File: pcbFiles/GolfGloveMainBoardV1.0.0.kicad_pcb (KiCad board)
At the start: 4 copper layers, 55.3 x 40 mm, 135 parts, among them J1 USB_C_Receptacle, J11 Conn_01x16_Male, J12 HOST_WAKE, J13 TP4, J14 Conn_01x02, J15 Conn_01x02, J16 Conn_01x02, J17 Conn_01x02, J2 Conn_01x06, J3 USB_C_Receptacle, J6 Screw_Terminal_01x02, J7 Conn_01x02, J8 Conn_01x02, J9 Conn_01x02, SW1 SW_SPDT, SW2 SW_Push, U1 MCP73831T-2ACI/OT, U2 XC6119N16A7R-G, U3 LSM9DS1TR, U4 CYW20719B1KUMLG, U5 LSM9DS1TR, U7 TPS63001DRCT, Y1 Crystal, Y3 Crystal_GND24

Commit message: Updates
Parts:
- removed C3, C4: C, Capacitors_SMD:C_0402
- removed J11: Conn_01x16_Male, Pin_Headers:Pin_Header_Straight_2x08_Pitch2.54mm
- removed J12: HOST_WAKE, Pin_Headers:Pin_Header_Straight_1x01_Pitch2.54mm
- removed J13: TP4, Pin_Headers:Pin_Header_Straight_1x01_Pitch2.54mm
- removed U2: XC6119N16A7R-G, DFN-4-------------------------:DFN-4
- added J4: Conn_01x02_Male, Pin_Headers:Pin_Header_Straight_1x02_Pitch2.54mm, F.Cu at (145.6, 147.0)
- added J5: Conn_01x02_Male, Pin_Headers:Pin_Header_Straight_1x02_Pitch2.54mm, F.Cu at (139.3, 146.8)
- added SW3: SW_Push_Dual, Buttons_Switches_THT:SW_PUSH_6mm, F.Cu at (127.5, 116.5)
- C8, C9, R3, R4: moved to F.Cu
- J6: value Screw_Terminal_01x02 -> Conn_01x02_Male
- SW2: footprint Buttons_Switches_SMD:SW_DIP_x1_W8.61mm_Slide_LowProfile -> Buttons_Switches_THT:SW_PUSH_6mm
- Y1: footprint Crystals:Crystal_SMD_0603-2pin_6.0x3.5mm_HandSoldering -> Crystals:Crystal_SMD_3215-2pin_3.2x1.5mm; moved to F.Cu
- Y3: footprint Crystals:Crystal_SMD_0603-4pin_6.0x3.5mm_HandSoldering -> Crystals:Crystal_SMD_2016-4pin_2.0x1.6mm
- moved J6 15.9 mm to (132.9, 147.0), turned to 0 degrees
- moved J17 7.00 mm to (122.5, 115.4)
- moved C9 5.58 mm to (132.2, 127.5), turned to 0 degrees
- moved SW2 5.08 mm to (113.8, 140.8)
- moved R4 3.55 mm to (132.8, 126.2), turned to 270 degrees
- moved Y1 3.34 mm to (134.6, 126.2), turned to 90 degrees
- moved Y3 3.30 mm to (122.3, 123.2)
- moved J2 3.24 mm to (126.5, 112.8)
- moved R3 2.59 mm to (125.2, 139.3)
- moved C8 2.52 mm to (132.2, 125.0), turned to 180 degrees
- moved C25 2.32 mm to (124.4, 123.2), turned to 90 degrees
- moved C23 2.21 mm to (120.3, 123.2), turned to 270 degrees
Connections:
- J6 pad 1: GND -> SDA
- J6 pad 2: Net-(C4-Pad2) -> SCLK
- R3 pad 2: Net-(C4-Pad2) -> RST_N
- SW2 pad 2: Net-(C4-Pad2) -> RST_N
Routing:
- net PSensor2: track 96.9 -> 52.3 mm, vias 8 -> 6
- net Sensor4: track 76.0 -> 35.2 mm
- net PSensor1: track 80.6 -> 48.5 mm, vias 8 -> 5
- net Sensor3: track 68.7 -> 40.9 mm, vias 3 -> 2
- net Sensor1: track 64.2 -> 42.1 mm
- net RST_N: track 22.9 -> 41.7 mm, vias 1 -> 2
- net Net-(C4-Pad2): track 17.9 -> 0.00 mm, vias 1 -> 0
- net Net-(U4-Pad24): track 17.2 -> 0.00 mm
- net GND: track 116.6 -> 130.8 mm, vias 14 -> 12
- net Net-(U4-Pad26): track 14.0 -> 0.00 mm
- net /BT_UART_CTS: track 18.3 -> 28.5 mm, vias 0 -> 2
- net Net-(C23-Pad1): track 38.7 -> 29.7 mm, vias 2 -> 4
- net Net-(C9-Pad2): track 15.1 -> 6.56 mm, vias 1 -> 0
- net BatteryOutBuck: track 39.5 -> 47.4 mm, vias 2 -> 3
- net Net-(J17-Pad2): track 5.59 -> 10.7 mm
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
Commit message: Ready For Review
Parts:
- added F1: Polyfuse, Resistors_SMD:R_0603_HandSoldering, F.Cu at (126.5, 149.5)
- added R14: R, Resistors_SMD:R_0402, B.Cu at (115.2, 131.5)
- added R16: R, Resistors_SMD:R_0402, B.Cu at (115.2, 130.5)
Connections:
- C37 pad 1: 3.3v -> Net-(C37-Pad1)
- C38 pad 1: 3.3v -> Net-(C37-Pad1)
- J1 pad A10: PSensor1 -> SDA
- J1 pad A11: PSensor2 -> PSensor1
- J1 pad A2: 3.3v -> PSensor2
- J1 pad A3: 3.3v -> SCLK
- J1 pad A6: SCLK -> Net-(J1-PadA6)
- J1 pad A7: SDA -> Net-(J1-PadA7)
- J1 pad A8: Net-(J1-PadA8) -> 3.3v
- J1 pad B10: Net-(J1-PadB10) -> SDA
- J1 pad B11: Net-(J1-PadB11) -> PSensor1
- J1 pad B2: 3.3v -> PSensor2
- J1 pad B3: 3.3v -> SCLK
- J1 pad B6: SCLK -> Net-(J1-PadB6)
- J1 pad B7: SDA -> Net-(J1-PadB7)
- J1 pad B8: Net-(J1-PadB8) -> 3.3v
- J3 pad A10: PSensor1 -> SDA-USB
- J3 pad A11: PSensor2 -> PSensor1
- J3 pad A2: USBVCC -> PSensor2
- J3 pad A3: USBVCC -> SCLK-USB
- J3 pad A6: SCLK-USB -> Net-(J3-PadA6)
- J3 pad A7: SDA-USB -> Net-(J3-PadA7)
- J3 pad A8: Net-(J3-PadA8) -> USBVCC
- J3 pad B10: PSensor1 -> SDA-USB
- J3 pad B11: PSensor2 -> PSensor1
- J3 pad B2: USBVCC -> PSensor2
- J3 pad B3: USBVCC -> SCLK-USB
- J3 pad B6: SCLK-USB -> Net-(J3-PadB6)
- J3 pad B7: SDA-USB -> Net-(J3-PadB7)
- J3 pad B8: Net-(J3-PadB8) -> USBVCC
- U3 pad 5: Net-(U3-Pad5) -> GND
- U3 pad 6: Net-(U3-Pad6) -> GND
- U3 pad 7: Net-(U3-Pad7) -> 3.3v
- U3 pad 8: Net-(U3-Pad8) -> 3.3v
- U5 pad 5: Net-(U5-Pad5) -> USBVCC
- U5 pad 6: Net-(U5-Pad6) -> USBVCC
- U5 pad 7: Net-(U5-Pad7) -> USBVCC
- U5 pad 8: Net-(U5-Pad8) -> USBVCC
- U7 pad 1: 3.3v -> Net-(C37-Pad1)
- U7 pad 10: 3.3v -> Net-(C37-Pad1)
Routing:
- net PSensor1: track 48.5 -> 76.3 mm
- net SDA: track 43.8 -> 69.9 mm, vias 5 -> 7
- net Net-(C37-Pad1): track 0.00 -> 23.8 mm, vias 0 -> 1
- net USBVCC: track 23.1 -> 40.9 mm, vias 2 -> 4
- net Net-(J1-PadA5): track 0.00 -> 16.0 mm, vias 0 -> 3
- net SCLK: track 47.5 -> 62.9 mm
- net SCLK-USB: track 4.50 -> 19.0 mm, vias 0 -> 3
- net GND: track 130.8 -> 141.9 mm
- net USBGND: track 19.8 -> 30.1 mm
- net 3.3v: track 338.4 -> 347.0 mm, vias 12 -> 11
- net PSensor2: track 52.3 -> 57.8 mm, vias 6 -> 3
- net Net-(J1-PadB5): track 0.00 -> 4.44 mm, vias 0 -> 1
- net SDA-USB: track 6.75 -> 8.70 mm

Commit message: Add LED for Power Indication
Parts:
- added D2: LED, Capacitors_SMD:C_0603, F.Cu at (127.0, 144.8)
- added R17: R, Resistors_SMD:R_0402, F.Cu at (124.4, 144.8)
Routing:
- net GND: track 141.9 -> 154.0 mm, vias 12 -> 13
- net 3.3v: track 347.0 -> 352.4 mm
- net Net-(D2-Pad2): track 0.00 -> 1.35 mm
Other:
- rule trace_min: 0.15 -> 0.0889
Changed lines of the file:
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@@
 (kicad_pcb (version 4) (host pcbnew 4.0.7)
   (general
-    (links 274)
-    (no_connects 4)
+    (links 277)
+    (no_connects 7)
     (area 93.529999 111.279999 149.000001 151.430001)
     (thickness 1.6)
     (drawings 32)
-    (tracks 1252)
+    (tracks 1266)
     (zones 0)
-    (modules 135)
-    (nets 84)
+    (modules 137)
+    (nets 85)
   )
   (page A4)
@@
     (zone_clearance 0.25)
     (zone_45_only yes)
-    (trace_min 0.15)
+    (trace_min 0.0889)
     (segment_width 0.2)
     (edge_width 0.15)
@@
   (net 82 "Net-(J3-PadA5)")
   (net 83 "Net-(J3-PadB5)")
+  (net 84 "Net-(D2-Pad2)")
   (net_class Default "This is the default net class."
     (clearance 0.15)
@@
     (add_net "Net-(D1-Pad1)")
     (add_net "Net-(D1-Pad2)")
+    (add_net "Net-(D2-Pad2)")
     (add_net "Net-(J1-PadA5)")
     (add_net "Net-(J1-PadA6)")
@@
     )
   )
+  (module Capacitors_SMD:C_0603 (layer F.Cu)
+    (at 126.95 144.75 180)
+    (descr "Capacitor SMD 0603, reflow soldering, AVX (see smccp.pdf)")
+    (tags "capacitor 0603")
+    (attr smd)
+    (fp_text reference D2 (at 0 -1.5 180) (layer F.SilkS)
+      (effects (font (size 1 1) (thickness 0.15)))
+    )
+    (fp_text value LED (at 0 1.5 180) (layer F.Fab)
+      (effects (font (size 1 1) (thickness 0.15)))
+    )
+    (fp_line (start 1.4 0.65) (end -1.4 0.65) (layer F.CrtYd) (width 0.05))
+    (fp_line (start 1.4 0.65) (end 1.4 -0.65) (layer F.CrtYd) (width 0.05))
+    (fp_line (start -1.4 -0.65) (end -1.4 0.65) (layer F.CrtYd) (width 0.05))
+    (fp_line (start -1.4 -0.65) (end 1.4 -0.65) (layer F.CrtYd) (width 0.05))
+    (fp_line (start 0.35 0.6) (end -0.35 0.6) (layer F.SilkS) (width 0.12))
+    (fp_line (start -0.35 -0.6) (end 0.35 -0.6) (layer F.SilkS) (width 0.12))
+    (fp_line (start -0.8 -0.4) (end 0.8 -0.4) (layer F.Fab) (width 0.1))
+    (fp_line (start 0.8 -0.4) (end 0.8 0.4) (layer F.Fab) (width 0.1))
+    (fp_line (start 0.8 0.4) (end -0.8 0.4) (layer F.Fab) (width 0.1))
+    (fp_line (start -0.8 0.4) (end -0.8 -0.4) (layer F.Fab) (width 0.1))
+    (fp_text user %R (at 0 0 180) (layer F.Fab)
+      (effects (font (size 0.3 0.3) (thickness 0.075)))
+    )
+    (pad 2 smd rect (at 0.75 0 180) (size 0.8 0.75) (layers F.Cu F.Paste F.Mask)
+      (net 84 "Net-(D2-Pad2)"))
+    (pad 1 smd rect (at -0.75 0 180) (size 0.8 0.75) (layers F.Cu F.Paste F.Mask)
+      (net 3 GND))
+    (model Capacitors_SMD.3dshapes/C_0603.wrl
+      (at (xyz 0 0 0))
+      (scale (xyz 1 1 1))
+      (rotate (xyz 0 0 0))
+    )
+  )
+  (module Resistors_SMD:R_0402 (layer F.Cu)
+    (at 124.4 144.75 180)
+    (descr "Resistor SMD 0402, reflow soldering, Vishay (see dcrcw.pdf)")
+    (tags "resistor 0402")
+    (attr smd)
+    (fp_text reference R17 (at 0 -1.35 180) (layer F.SilkS)
+      (effects (font (size 1 1) (thickness 0.15)))
+    )
+    (fp_text value R (at 0 1.45 180) (layer F.Fab)
+      (effects (font (size 1 1) (thickness 0.15)))
+    )
+    (fp_text user %R (at 0 -1.35 180) (layer F.Fab)
+      (effects (font (size 1 1) (thickness 0.15)))
+    )
+    (fp_line (start -0.5 0.25) (end -0.5 -0.25) (layer F.Fab) (width 0.1))
+    (fp_line (start 0.5 0.25) (end -0.5 0.25) (layer F.Fab) (width 0.1))
+    (fp_line (start 0.5 -0.25) (end 0.5 0.25) (layer F.Fab) (width 0.1))
+    (fp_line (start -0.5 -0.25) (end 0.5 -0.25) (layer F.Fab) (width 0.1))
+    (fp_line (start 0.25 -0.53) (end -0.25 -0.53) (layer F.SilkS) (width 0.12))
+    (fp_line (start -0.25 0.53) (end 0.25 0.53) (layer F.SilkS) (width 0.12))
+    (fp_line (start -0.8 -0.45) (end 0.8 -0.45) (layer F.CrtYd) (width 0.05))
+    (fp_line (start -0.8 -0.45) (end -0.8 0.45) (layer F.CrtYd) (width 0.05))
+    (fp_line (start 0.8 0.45) (end 0.8 -0.45) (layer F.CrtYd) (width 0.05))
+    (fp_line (start 0.8 0.45) (end -0.8 0.45) (layer F.CrtYd) (width 0.05))
+    (pad 1 smd rect (at -0.45 0 180) (size 0.4 0.6) (layers F.Cu F.Paste F.Mask)
+      (net 84 "Net-(D2-Pad2)"))
+    (pad 2 smd rect (at 0.45 0 180) (size 0.4 0.6) (layers F.Cu F.Paste F.Mask)
+      (net 5 3.3v))
+    (model ${KISYS3DMOD}/Resistors_SMD.3dshapes/R_0402.wrl
+      (at (xyz 0 0 0))
+      (scale (xyz 1 1 1))
+      (rotate (xyz 0 0 0))
+    )
+  )
   (gr_text REV1.0 (at 120.65 111.65 90) (layer B.SilkS)
     (effects (font (size 1.5 1.5) (thickness 0.3)) (justify mirror))
@@
   (segment (start 130.9675 137.2025) (end 130.9675 138.2173) (width 0.25) (layer F.Cu) (net 2))
   (segment (start 130.9675 138.2173) (end 130.7971 138.3877) (width 0.25) (layer F.Cu) (net 2))
-  (segment (start 114.715 130.519999) (end 113.630001 130.519999) (width 0.15) (layer B.Cu) (net 3) (status 400000))
-  (segment (start 113.630001 130.519999) (end 113.225 130.925) (width 0.15) (layer B.Cu) (net 3) (status 800000))
-  (segment (start 114.715 130.519999) (end 114.715 131.485) (width 0.15) (layer B.Cu) (net 3) (status C00000))
-  (segment (start 114.715 131.485) (end 114.7 131.5) (width 0.15) (layer B.Cu) (net 3) (status C00000))
+  (segment (start 120.25 140.85) (end 120.25 141.2) (width 0.15) (layer B.Cu) (net 3) (status C00000))
+  (segment (start 120.25 141.2) (end 122.3 143.25) (width 0.15) (layer B.Cu) (net 3) (status 400000))
+  (segment (start 128.9 144.75) (end 127.7 144.75) (width 0.15) (layer F.Cu) (net 3) (status 800000))
+  (segment (start 128.95 144.8) (end 128.9 144.75) (width 0.15) (layer F.Cu) (net 3))
+  (via (at 128.95 144.8) (size 0.45) (drill 0.2) (layers F.Cu B.Cu) (net 3))
+  (segment (start 128.95 144.35) (end 128.95 144.8) (width 0.15) (layer B.Cu) (net 3))
+  (segment (start 128.4 143.8) (end 128.95 144.35) (width 0.15) (layer B.Cu) (net 3))
+  (segment (start 127.35 143.8) (end 128.4 143.8) (width 0.15) (layer B.Cu) (net 3))
+  (segment (start 126.8 143.25) (end 127.35 143.8) (width 0.15) (layer B.Cu) (net 3))
+  (segment (start 122.3 143.25) (end 126.8 143.25) (width 0.15) (layer B.Cu) (net 3))
+  (segment (start 114.715 130.519999) (end 113.630001 130.519999) (width 0.15) (layer B.Cu) (net 3))
+  (segment (start 113.630001 130.519999) (end 113.225 130.925) (width 0.15) (layer B.Cu) (net 3))
+  (segment (start 114.715 130.519999) (end 114.715 131.485) (width 0.15) (layer B.Cu) (net 3))
+  (segment (start 114.715 131.485) (end 114.7 131.5) (width 0.15) (layer B.Cu) (net 3))
   (segment (start 120.085 128.45) (end 120.085 128.385) (width 0.15) (layer F.Cu) (net 3))
   (segment (start 120.085 128.385) (end 119.485 127.785) (width 0.15) (layer F.Cu) (net 3))
@@
   (segment (start 135.335 137.255) (end 135.335 139.475) (width 0.2) (layer F.Cu) (net 4))
   (segment (start 134.635 136.555) (end 135.335 137.255) (width 0.2) (layer F.Cu) (net 4))
-  (segment (start 121.395 132) (end 122.1 132) (width 0.3) (layer F.Cu) (net 5) (status 400000))
+  (segment (start 125.35 149.5) (end 125.35 147.45) (width 0.3) (layer F.Cu) (net 5) (status 400000))
+  (segment (start 123.95 146.05) (end 123.95 144.75) (width 0.3) (layer F.Cu) (net 5) (status 800000))
+  (segment (start 125.35 147.45) (end 123.95 146.05) (width 0.3) (layer F.Cu) (net 5))
+  (segment (start 121.395 132) (end 122.1 132) (width 0.3) (layer F.Cu) (net 5))
   (segment (start 124.3 128.5) (end 123.3825 127.5825) (width 0.3) (layer In2.Cu) (net 5))
   (segment (start 124.3 130.6) (end 124.3 128.5) (width 0.3) (layer In2.Cu) (net 5))
@@
   (segment (start 100.925 131.045) (end 100.96 131.01) (width 0.25) (layer F.Cu) (net 77))
   (segment (start 102.08 130.86) (end 102.27 130.86) (width 0.25) (layer F.Cu) (net 78))
-  (segment (start 121.395 130.5) (end 122.35 130.5) (width 0.15) (layer F.Cu) (net 80) (status 400000))
-  (segment (start 116.2 131.5) (end 115.6 131.5) (width 0.15) (layer B.Cu) (net 80) (status 800000))
+  (segment (start 121.395 130.5) (end 122.35 130.5) (width 0.15) (layer F.Cu) (net 80))
+  (segment (start 116.2 131.5) (end 115.6 131.5) (width 0.15) (layer B.Cu) (net 80))
   (segment (start 116.3 131.6) (end 116.2 131.5) (width 0.15) (layer B.Cu) (net 80))
   (via (at 116.3 131.6) (size 0.45) (drill 0.2) (layers F.Cu B.Cu) (net 80))
@@
   (via (at 122.4 130.55) (size 0.45) (drill 0.2) (layers F.Cu B.Cu) (net 80))
   (segment (start 122.35 130.5) (end 122.4 130.55) (width 0.15) (layer F.Cu) (net 80))
-  (segment (start 115.615 130.519999) (end 116.419999 130.519999) (width 0.15) (layer B.Cu) (net 81) (status 400000))
-  (segment (start 118.55 131.5) (end 119.1 132.05) (width 0.15) (layer F.Cu) (net 81) (status 800000))
+  (segment (start 115.615 130.519999) (end 116.419999 130.519999) (width 0.15) (layer B.Cu) (net 81))
+  (segment (start 118.55 131.5) (end 119.1 132.05) (width 0.15) (layer F.Cu) (net 81))
   (segment (start 117.4 131.5) (end 118.55 131.5) (width 0.15) (layer F.Cu) (net 81))
   (via (at 117.4 131.5) (size 0.45) (drill 0.2) (layers F.Cu B.Cu) (net 81))
   (segment (start 116.419999 130.519999) (end 117.4 131.5) (width 0.15) (layer B.Cu) (net 81))
-  (segment (start 119.1 132.05) (end 119.385 132.05) (width 0.15) (layer F.Cu) (net 81) (status C00000))
+  (segment (start 119.1 132.05) (end 119.385 132.05) (width 0.15) (layer F.Cu) (net 81))
   (segment (start 119.385 132.05) (end 119.35 132.05) (width 0.3) (layer In2.Cu) (net 81))
+  (segment (start 126.2 144.75) (end 124.85 144.75) (width 0.15) (layer F.Cu) (net 84) (status C00000))
   (zone (net 0) (net_name "") (layer F.Cu) (hatch edge 0.508)
     (connect_pads (clearance 0.508))
@@
     (connect_pads (clearance 0.25))
     (min_thickness 0.254)
-    (fill yes (arc_segments 16) (thermal_gap 0.508) (thermal_bridge_width 0.508))
+    (fill (arc_segments 16) (thermal_gap 0.508) (thermal_bridge_width 0.508))
     (polygon
       (pts
@@
     (connect_pads (clearance 0.25))
     (min_thickness 0.254)
-    (fill yes (arc_segments 16) (thermal_gap 0.508) (thermal_bridge_width 0.508))
+    (fill (arc_segments 16) (thermal_gap 0.508) (thermal_bridge_width 0.508))
     (polygon
       (pts

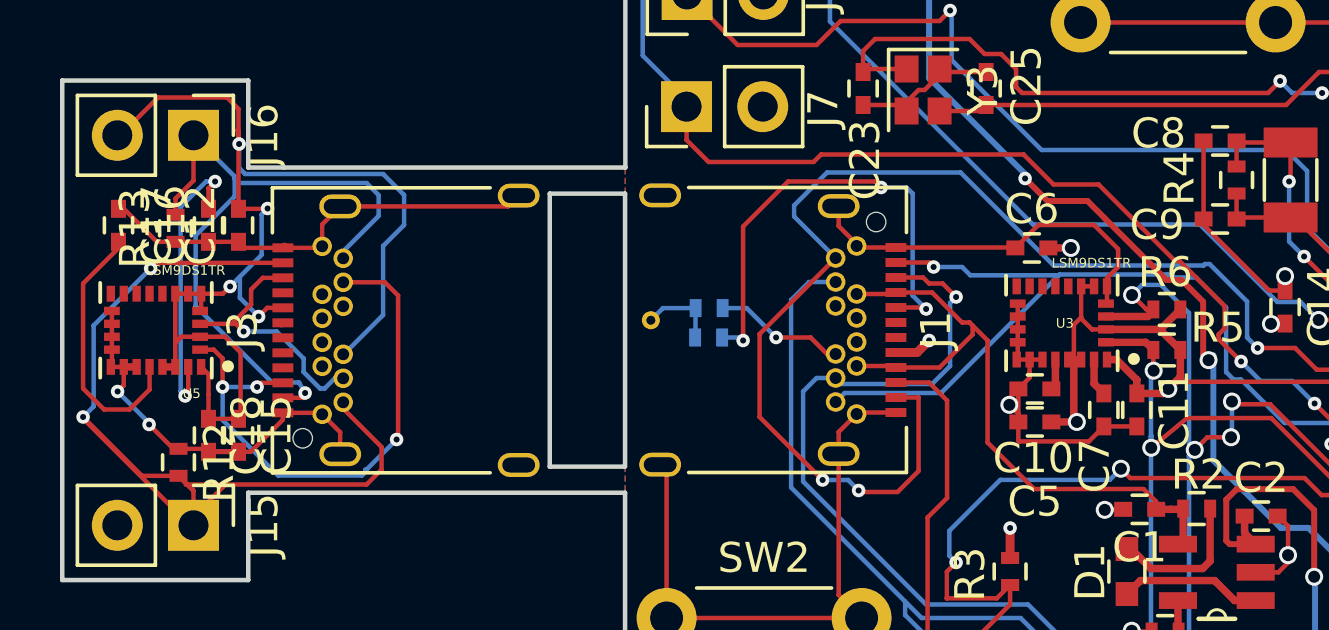
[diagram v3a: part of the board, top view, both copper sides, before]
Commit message: Fix LSM footprints
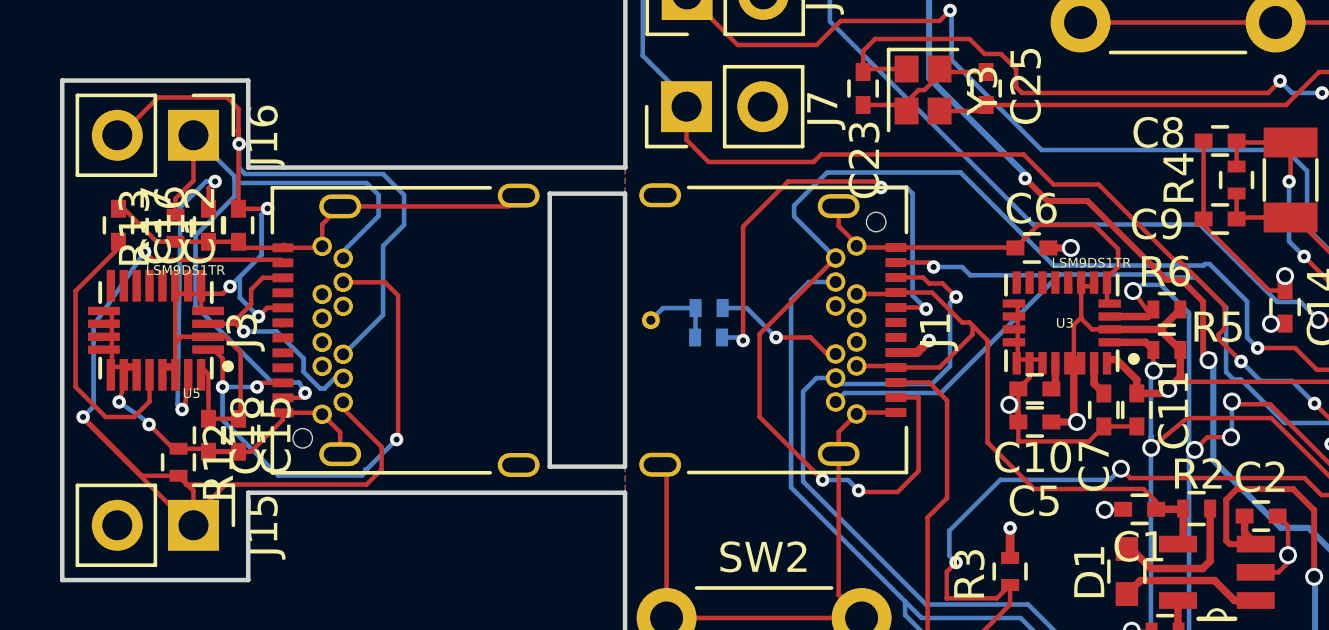
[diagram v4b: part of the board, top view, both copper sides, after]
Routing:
- net Net-(C16-Pad2): track 9.88 -> 10.8 mm
- net Net-(C17-Pad2): track 8.91 -> 9.68 mm

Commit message: Update
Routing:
- net USBGND: track 30.1 -> 39.8 mm
- net PSensor1: track 76.8 -> 74.5 mm
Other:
- outline, holes or cut-outs redrawn
- board text added: "REV2.0"
- board text added: "y33t"
